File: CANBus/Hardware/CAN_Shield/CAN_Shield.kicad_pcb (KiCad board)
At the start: 2 copper layers, 101.6 x 53.3 mm, 20 parts, among them J1 Power, J2 PWM, J3 Analog, J4 PWM, J5 Analog, J6 Communication, J7 Digital, J8 Screw_Terminal_01x02, U2 TCAN1051HGV

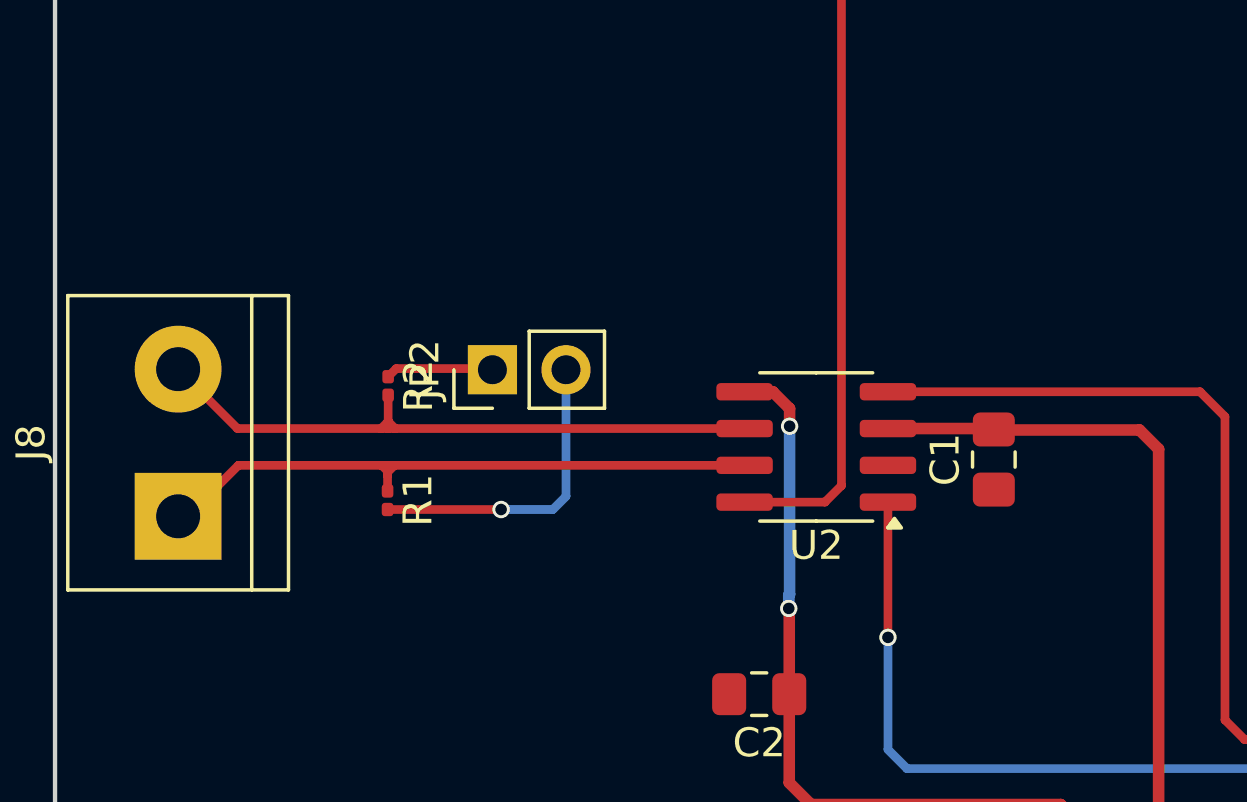
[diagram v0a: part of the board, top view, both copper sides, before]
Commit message: feat: Resistors got changed
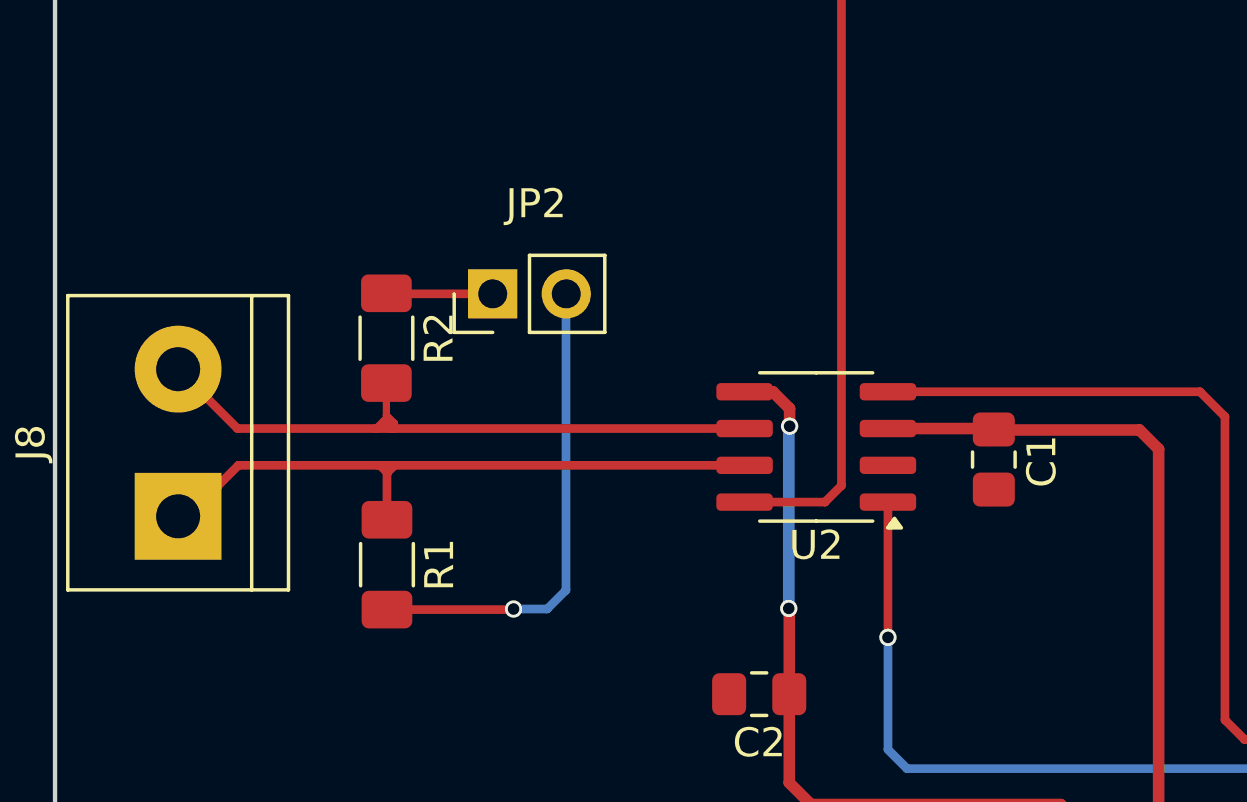
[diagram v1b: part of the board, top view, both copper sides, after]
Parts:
- R1, R2: footprint Resistor_SMD:R_0201_0603Metric -> Resistor_SMD:R_1206_3216Metric_Pad1.30x1.75mm_HandSolder
- moved JP2 2.62 mm to (115.1, 72.0)
- moved R1 2.23 mm to (111.5, 81.3)
- moved R2 1.65 mm to (111.4, 73.5)
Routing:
- net Net-(JP2-B): track 10.7 -> 16.7 mm
- net Net-(J8-Pin_1): track 21.8 -> 22.9 mm
- net Net-(J8-Pin_2): track 22.3 -> 23.1 mm

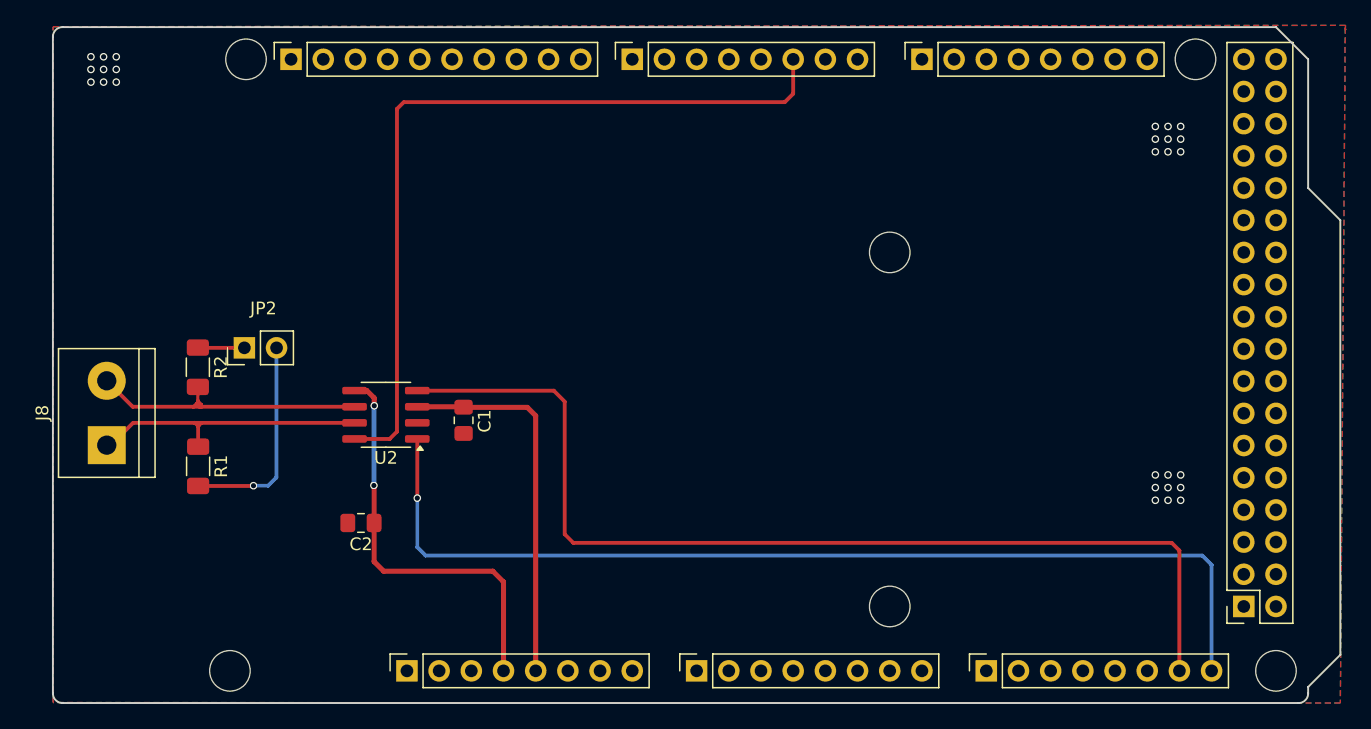
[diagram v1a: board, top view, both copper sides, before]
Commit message: feat(Hw): Route PCB
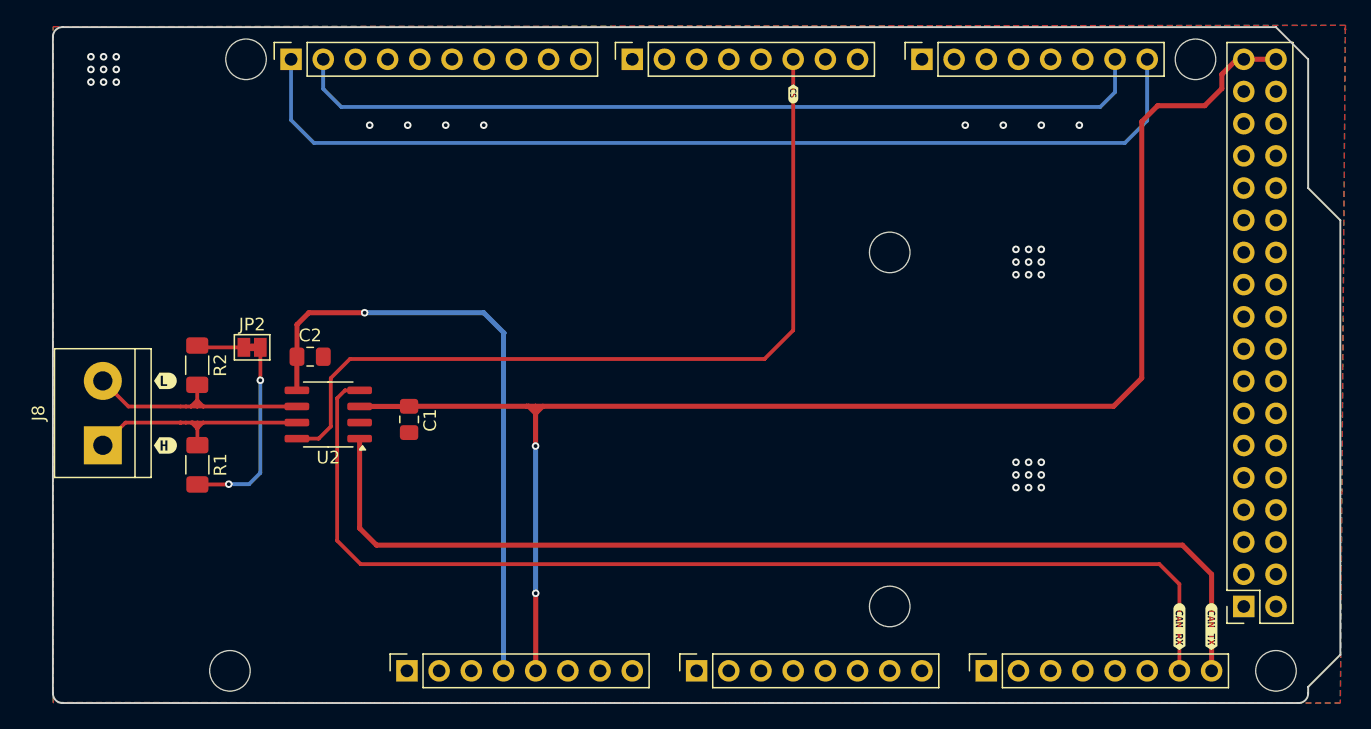
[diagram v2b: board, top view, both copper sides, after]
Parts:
- added kibuzzard-66170297: G***, kibuzzard-66170297, F.Cu at (191.4, 94.0)
- added kibuzzard-661702AA: G***, kibuzzard-661702AA, F.Cu at (188.9, 94.0)
- added kibuzzard-661702C6: G***, kibuzzard-661702C6, F.Cu at (158.4, 51.9)
- added kibuzzard-66170410: G***, kibuzzard-66170410, F.Cu at (108.9, 79.7)
- added kibuzzard-6617048F: G***, kibuzzard-6617048F, F.Cu at (108.9, 74.6)
- JP2: footprint Connector_PinHeader_2.54mm:PinHeader_1x02_P2.54mm_Vertical -> Jumper:SolderJumper-2_P1.3mm_Bridged_Pad1.0x1.5mm
- moved C2 13.7 mm to (120.3, 72.7), turned to 0 degrees
- moved U2 4.55 mm to (121.7, 77.2)
- moved C1 4.30 mm to (128.1, 77.6)
- moved JP2 0.61 mm to (115.7, 71.9), turned to 0 degrees
- moved J8 0.31 mm to (103.9, 79.7)
- moved R2 0.17 mm to (111.4, 73.3)
- moved R1 0.13 mm to (111.4, 81.2)
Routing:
- net +5V: track 29.8 -> 118.8 mm, vias 0 -> 2
- net /SCL/21: track 0.00 -> 78.7 mm
- net /SDA/20: track 0.00 -> 68.5 mm
- net +3V3: track 32.6 -> 49.3 mm, vias 2 -> 1
- net /CANRX0_DUE/GIGA: track 81.0 -> 88.0 mm
- net Net-(J8-Pin_2): track 23.1 -> 19.2 mm
- net Net-(J8-Pin_1): track 22.9 -> 19.3 mm
- net /CANTX0_DUE/GIGA: track 80.2 -> 83.4 mm, vias 1 -> 0
- net /*2: track 63.5 -> 66.3 mm
- net Net-(JP2-B): track 16.7 -> 15.3 mm, vias 1 -> 2
- net GND: vias 27 -> 35

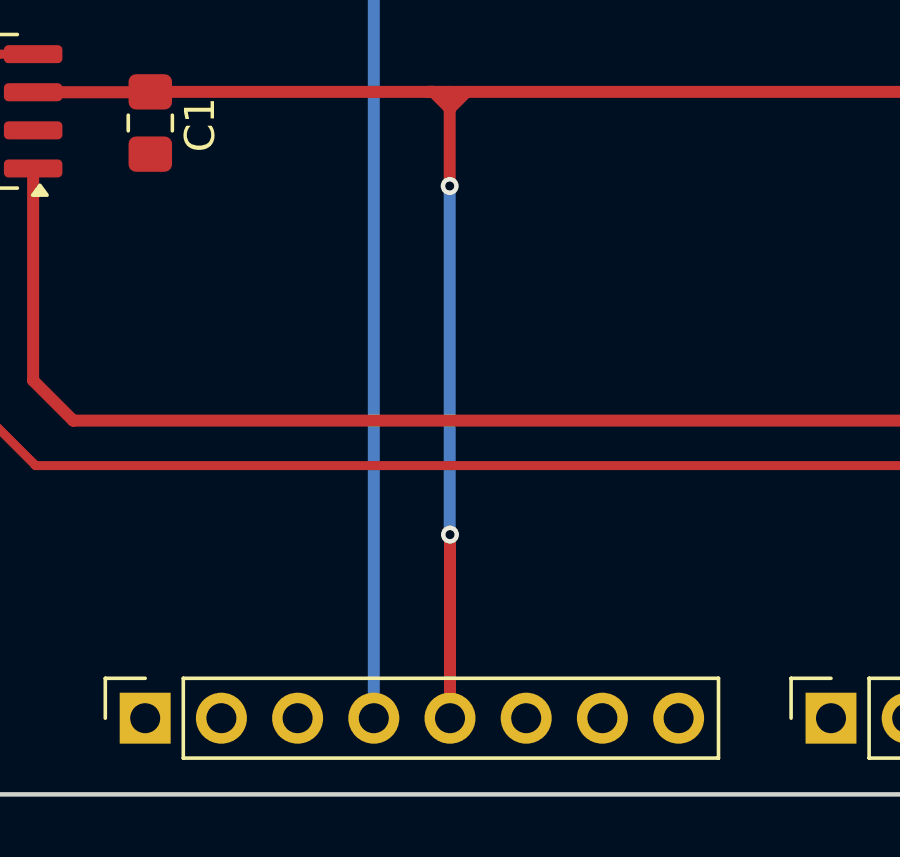
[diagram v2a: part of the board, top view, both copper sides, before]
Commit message: feat(Hw): Update route
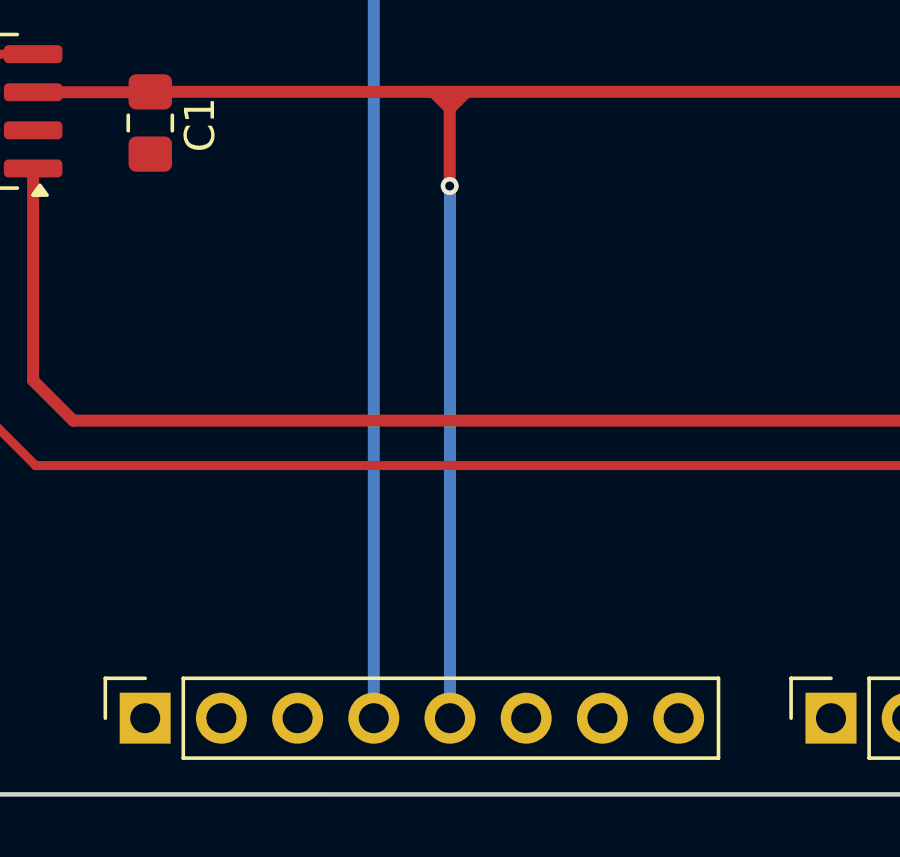
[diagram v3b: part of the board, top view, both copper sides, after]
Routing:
- net +5V: vias 2 -> 1
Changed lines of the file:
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@@
-	)
-	(segment
-		(start 138.1 91.34)
-		(end 138.1 97.46)
-		(width 0.4)
-		(layer "F.Cu")
-		(net 34)
 	)
 	(segment
@@
 		(net 34)
 	)
-	(via
-		(at 138.1 91.34)
-		(size 0.6)
-		(drill 0.3)
-		(layers "F.Cu" "B.Cu")
-		(net 34)
-	)
 	(segment
 		(start 138.09 79.72)
-		(end 138.09 91.33)
+		(end 138.1 79.73)
 		(width 0.4)
 		(layer "B.Cu")
@@
 	)
 	(segment
-		(start 138.09 91.33)
-		(end 138.1 91.34)
+		(start 138.1 79.73)
+		(end 138.1 97.46)
 		(width 0.4)
 		(layer "B.Cu")

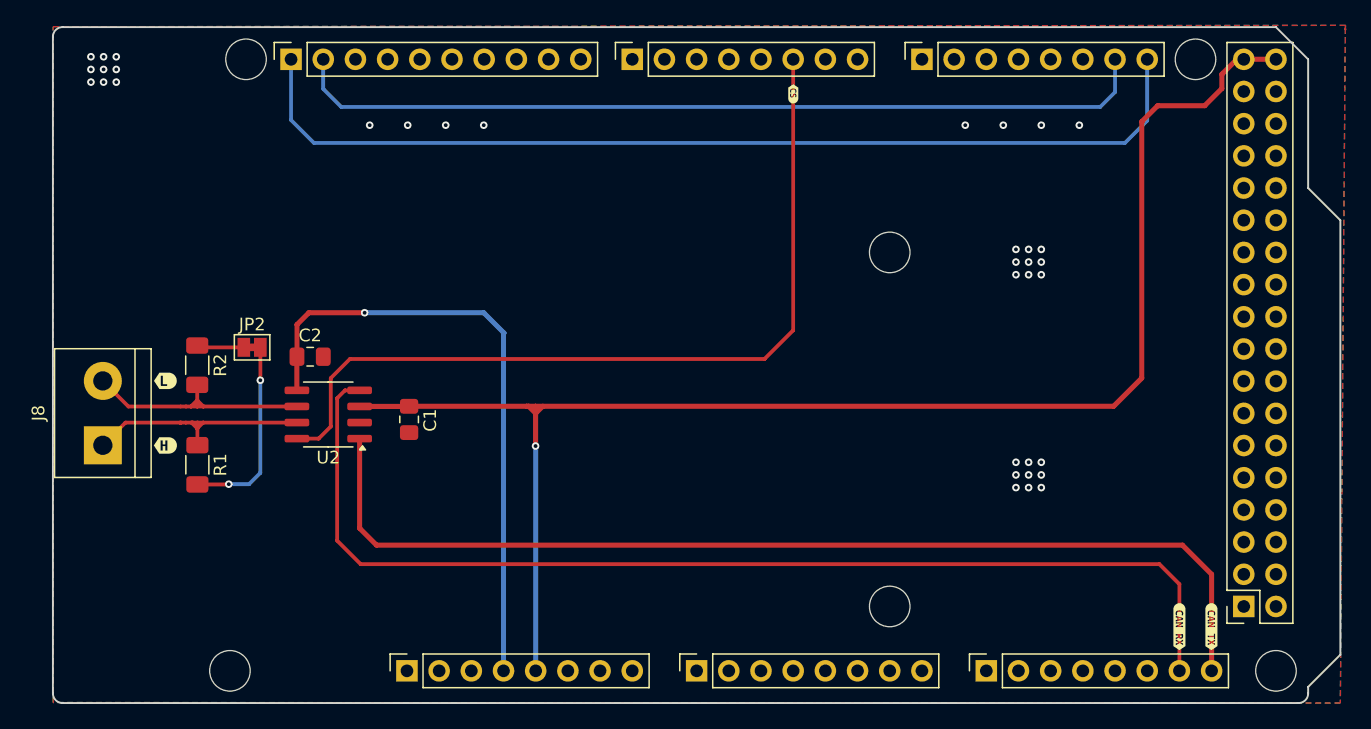
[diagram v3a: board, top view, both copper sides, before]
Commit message: feat(hw): add logos and labels for MEGA
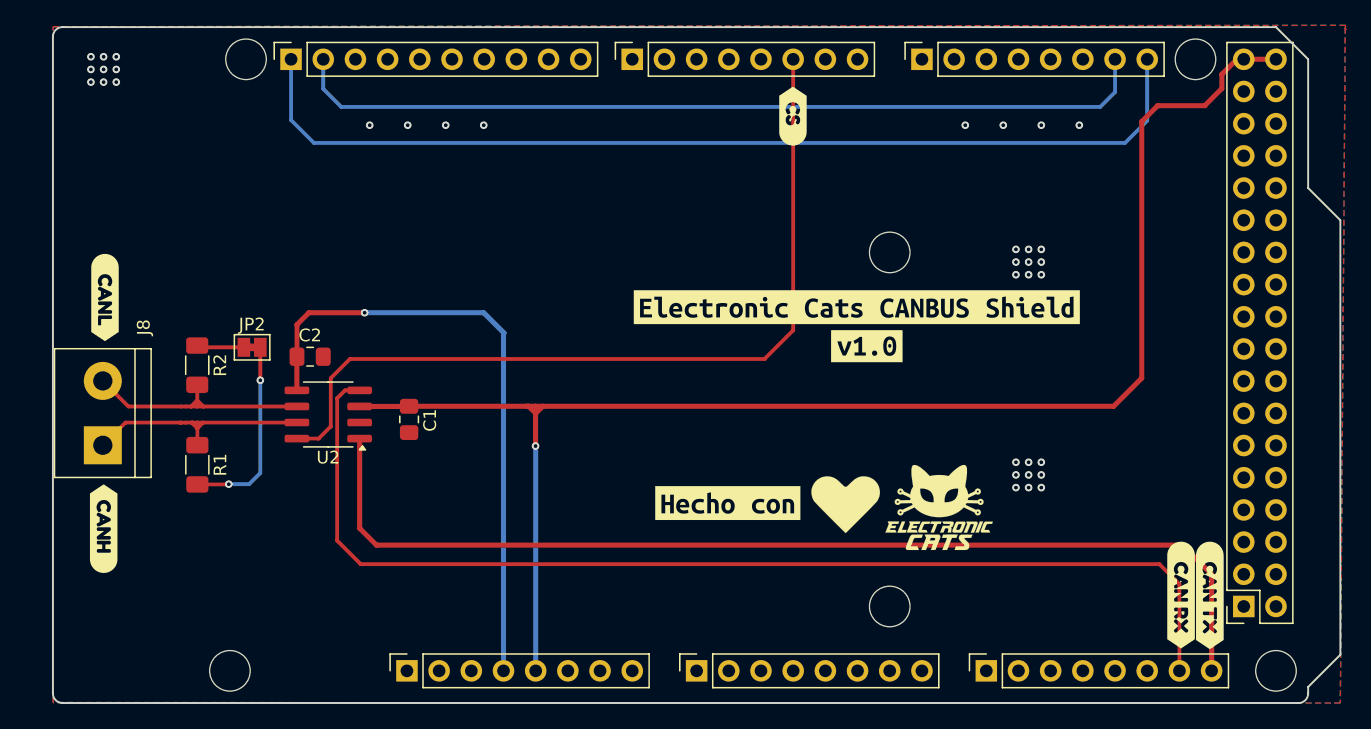
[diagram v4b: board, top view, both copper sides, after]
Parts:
- removed kibuzzard-66170297: G***, kibuzzard-66170297
- removed kibuzzard-661702AA: G***, kibuzzard-661702AA
- removed kibuzzard-661702C6: G***, kibuzzard-661702C6
- removed kibuzzard-66170410: G***, kibuzzard-66170410
- removed kibuzzard-6617048F: G***, kibuzzard-6617048F
- added G***: LOGO, Aesthetics:electronic_cats_logo_8x6, F.Cu at (169.9, 84.6)
- added G***: LOGO, Aesthetics:electronic_cats_logo_8x6, B.Cu at (151.9, 84.6)
- added Ref**: Val**, Aesthetics:heart, F.Cu at (159.8, 84.8)
- added Ref**: Val**, Aesthetics:heart, B.Cu at (162.6, 84.4)
- added kibuzzard-661820F9: G***, kibuzzard-661820F9, F.Cu at (153.3, 84.2)
- added kibuzzard-661820F9: G***, kibuzzard-661820F9, B.Cu at (169.3, 84.4)
- added kibuzzard-66182154: G***, kibuzzard-66182154, F.Cu at (163.4, 68.8)
- added kibuzzard-66182154: G***, kibuzzard-66182154, B.Cu at (163.4, 68.8)
- added kibuzzard-6618216B: G***, kibuzzard-6618216B, F.Cu at (164.2, 71.8)
- added kibuzzard-6618216B: G***, kibuzzard-6618216B, B.Cu at (164.2, 71.8)
- added kibuzzard-661821F7: G***, kibuzzard-661821F7, F.Cu at (158.4, 53.7)
- added kibuzzard-66182200: G***, kibuzzard-66182200, F.Cu at (189.0, 91.5)
- added kibuzzard-66182208: G***, kibuzzard-66182208, F.Cu at (191.3, 91.5)
- added kibuzzard-66182264: G***, kibuzzard-66182264, F.Cu at (104.0, 86.2)
- added kibuzzard-66182281: G***, kibuzzard-66182281, F.Cu at (104.1, 68.0)

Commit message: fix(hw): orientation labels MEGA
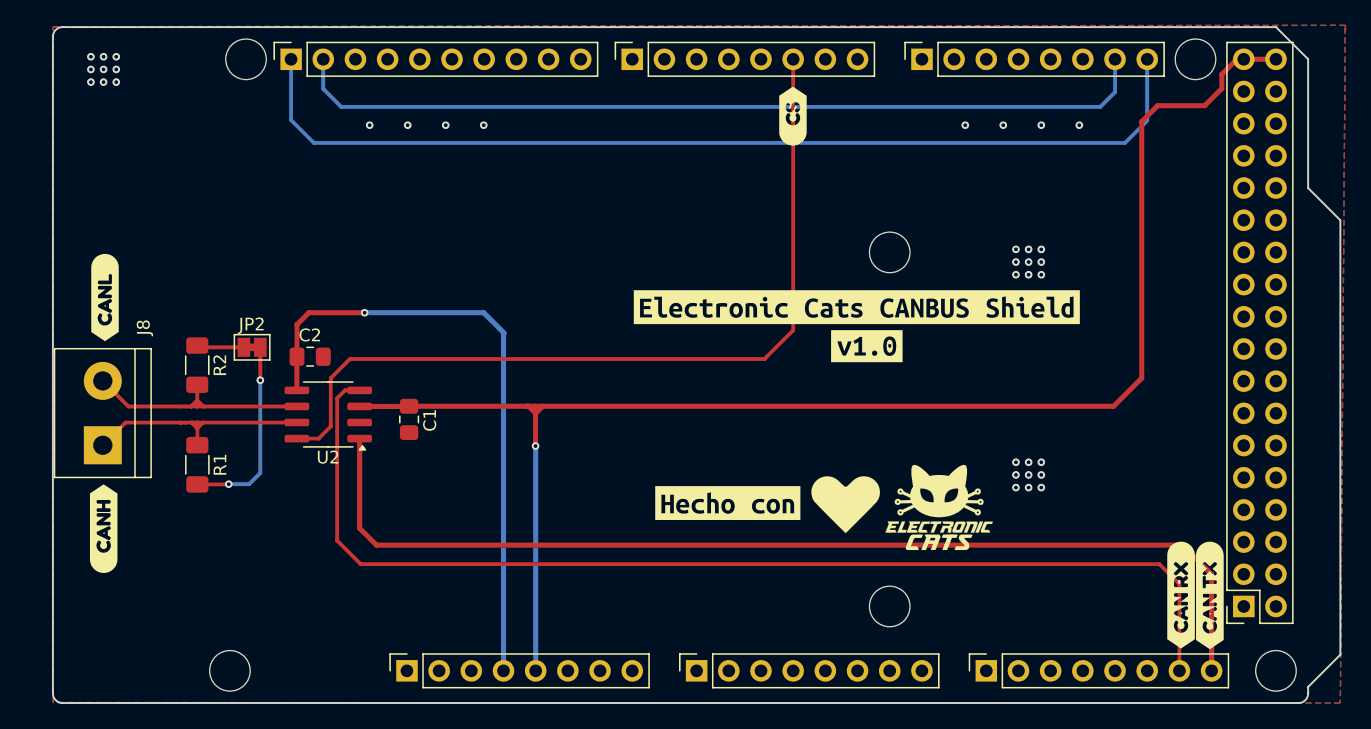
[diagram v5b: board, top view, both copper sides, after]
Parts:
- removed kibuzzard-661821F7: G***, kibuzzard-661821F7
- removed kibuzzard-66182200: G***, kibuzzard-66182200
- removed kibuzzard-66182208: G***, kibuzzard-66182208
- removed kibuzzard-66182264: G***, kibuzzard-66182264
- removed kibuzzard-66182281: G***, kibuzzard-66182281
- added kibuzzard-661834CB: G***, kibuzzard-661834CB, F.Cu at (158.4, 53.7)
- added kibuzzard-661834DA: G***, kibuzzard-661834DA, F.Cu at (191.3, 91.5)
- added kibuzzard-661834E4: G***, kibuzzard-661834E4, F.Cu at (189.0, 91.5)
- added kibuzzard-66183501: G***, kibuzzard-66183501, F.Cu at (104.1, 68.0)
- added kibuzzard-6618350C: G***, kibuzzard-6618350C, F.Cu at (104.0, 86.2)
